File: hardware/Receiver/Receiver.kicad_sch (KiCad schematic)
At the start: 132 parts, among them J1 USB_C_Receptacle_USB2.0, J3 20021511-00006T4LF, J4 Conn_01x04, J6 JST_PH, Q1 2N7002, Q2 NMOS, Q3 NMOS, Q4 PMOS, SW1 Boot, SW1 Reset, SW3 1825027-8, U1 TPS22810DRV, U2 DMG6602SVTQ, U2 TPS22810DRV, U3 AZ1117-3.3, U3 DMG6602SVTQ, U4 TLV493DA1B6HTSA2, U6 BQ76905, U8 ESP32-S3-MINI-1-N8

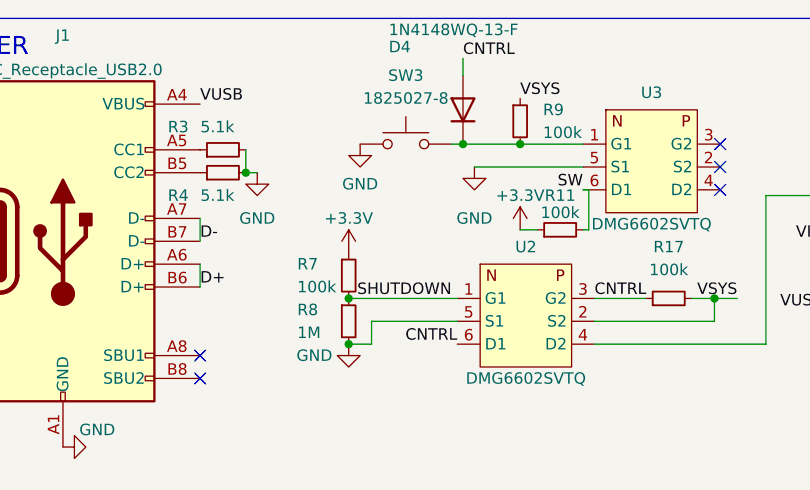
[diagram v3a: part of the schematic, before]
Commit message: add tvs diodes
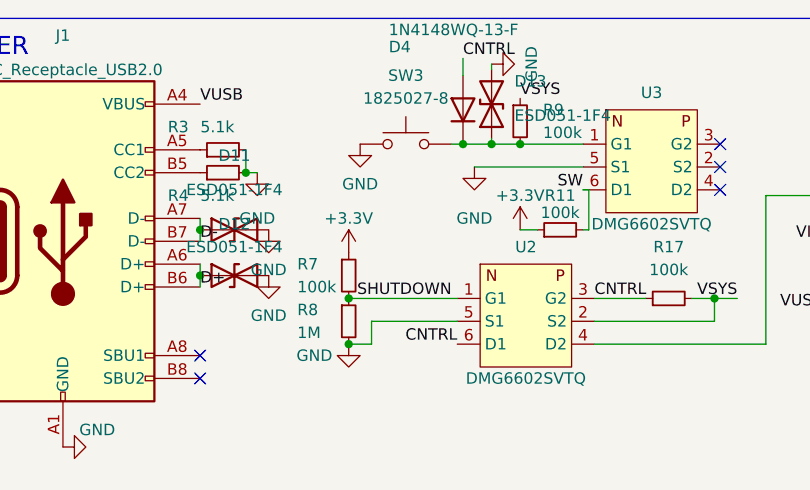
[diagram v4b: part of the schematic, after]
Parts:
- added D11, D12, D13: ESD051-1F4, Diode_SMD:D_0201_0603Metric, symbol Device:D_TVS
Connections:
- net D+: now also D12.1 (A1)
- net D-: now also D11.1 (A1)
- net GND: now also D11.2 (A2), D12.2 (A2), D13.2 (A2)
- net at D4.1 (K), R9.2, SW3.2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: now also D13.1 (A1)
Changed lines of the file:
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@@
   (junction (at 94.615 117.475) (diameter 0) (color 0 0 0 0)
   )
+  (junction (at 78.74 29.21) (diameter 0) (color 0 0 0 0)
+  )
   (junction (at 32.385 120.015) (diameter 0) (color 0 0 0 0)
   )
@@
   (junction (at 103.505 46.355) (diameter 0) (color 0 0 0 0)
   )
+  (junction (at 46.355 38.735) (diameter 0) (color 0 0 0 0)
+  )
   (junction (at 71.12 83.185) (diameter 0) (color 0 0 0 0)
   )
@@
   (junction (at 75.565 29.21) (diameter 0) (color 0 0 0 0)
   )
+  (junction (at 46.355 43.815) (diameter 0) (color 0 0 0 0)
+  )
   (junction (at 97.155 126.365) (diameter 0) (color 0 0 0 0)
   )
@@
     (stroke (width 0) (type default))
   )
-  (wire (pts (xy 75.565 29.21) (xy 81.915 29.21))
+  (wire (pts (xy 75.565 29.21) (xy 78.74 29.21))
     (stroke (width 0) (type default))
   )
@@
     (stroke (width 0) (type default))
   )
+  (wire (pts (xy 78.74 29.21) (xy 81.915 29.21))
+    (stroke (width 0) (type default))
+  )
   (wire (pts (xy 102.87 175.895) (xy 80.645 175.895))
     (stroke (width 0) (type default))
@@
     (stroke (width 0) (type default))
   )
+  (wire (pts (xy 46.355 38.735) (xy 46.355 40.005))
+    (stroke (width 0) (type default))
+  )
   (wire (pts (xy 39.37 141.605) (xy 43.18 141.605))
     (stroke (width 0) (type default))
@@
     (stroke (width 0) (type default))
   )
+  (wire (pts (xy 46.355 43.815) (xy 46.355 45.085))
+    (stroke (width 0) (type default))
+  )
   (wire (pts (xy 109.22 34.925) (xy 124.46 34.925))
     (stroke (width 0) (type default))
@@
     (stroke (width 0) (type default))
   )
-  (wire (pts (xy 46.355 37.465) (xy 46.355 40.005))
+  (wire (pts (xy 46.355 37.465) (xy 46.355 38.735))
     (stroke (width 0) (type default))
   )
@@
     (stroke (width 0) (type default))
   )
+  (wire (pts (xy 78.74 28.575) (xy 78.74 29.21))
+    (stroke (width 0) (type default))
+  )
   (wire (pts (xy 129.54 41.275) (xy 129.54 42.545))
     (stroke (width 0) (type default))
@@
     (stroke (width 0) (type default))
   )
-  (wire (pts (xy 46.355 42.545) (xy 46.355 45.085))
+  (wire (pts (xy 46.355 42.545) (xy 46.355 43.815))
     (stroke (width 0) (type default))
   )
@@
     (stroke (width 0) (type default))
   )
+  (wire (pts (xy 78.74 20.32) (xy 78.74 20.955))
+    (stroke (width 0) (type default))
+  )
   (wire (pts (xy 80.645 136.525) (xy 93.345 136.525))
     (stroke (width 0) (type default))
@@
     )
   )
+  (symbol (lib_id "power:GND") (at 53.975 38.735 0) (unit 1)
+    (in_bom yes) (on_board yes) (dnp no) (fields_autoplaced)
+    (property "Reference" "#PWR075" (at 53.975 45.085 0)
+      (effects (font (size 1.27 1.27)) hide)
+    )
+    (property "Value" "GND" (at 53.975 43.18 0)
+      (effects (font (size 1.27 1.27)))
+    )
+    (property "Footprint" "" (at 53.975 38.735 0)
+      (effects (font (size 1.27 1.27)) hide)
+    )
+    (property "Datasheet" "" (at 53.975 38.735 0)
+      (effects (font (size 1.27 1.27)) hide)
+    )
+    (pin "1")
+    (instances
+      (project "Receiver"
+        (path "/65c9fdc5-280c-4d5e-b4cf-324fcb70d6aa"
+          (reference "#PWR075") (unit 1)
+        )
+      )
+    )
+  )
   (symbol (lib_id "power:GND") (at 233.68 148.59 0) (unit 1)
     (in_bom yes) (on_board yes) (dnp no) (fields_autoplaced)
@@
     )
   )
+  (symbol (lib_id "Device:D_TVS") (at 50.165 38.735 0) (unit 1)
+    (in_bom yes) (on_board yes) (dnp no) (fields_autoplaced)
+    (property "Reference" "D11" (at 50.165 30.48 0)
+      (effects (font (size 1.27 1.27)))
+    )
+    (property "Value" "	\nESD051-1F4" (at 50.165 34.29 0)
+      (effects (font (size 1.27 1.27)))
+    )
+    (property "Footprint" "Diode_SMD:D_0201_0603Metric" (at 50.165 38.735 0)
+      (effects (font (size 1.27 1.27)) hide)
+    )
+    (property "Datasheet" "~" (at 50.165 38.735 0)
+      (effects (font (size 1.27 1.27)) hide)
+    )
+    (pin "1")
+    (pin "2")
+    (instances
+      (project "Receiver"
+        (path "/65c9fdc5-280c-4d5e-b4cf-324fcb70d6aa"
+          (reference "D11") (unit 1)
+        )
+      )
+    )
+  )
   (symbol (lib_id "power:+3.3V") (at 224.155 138.43 0) (unit 1)
     (in_bom yes) (on_board yes) (dnp no) (fields_autoplaced)
@@
     )
   )
+  (symbol (lib_id "power:GND") (at 78.74 20.32 90) (unit 1)
+    (in_bom yes) (on_board yes) (dnp no) (fields_autoplaced)
+    (property "Reference" "#PWR076" (at 85.09 20.32 0)
+      (effects (font (size 1.27 1.27)) hide)
+    )
+    (property "Value" "GND" (at 83.185 20.32 0)
+      (effects (font (size 1.27 1.27)))
+    )
+    (property "Footprint" "" (at 78.74 20.32 0)
+      (effects (font (size 1.27 1.27)) hide)
+    )
+    (property "Datasheet" "" (at 78.74 20.32 0)
+      (effects (font (size 1.27 1.27)) hide)
+    )
+    (pin "1")
+    (instances
+      (project "Receiver"
+        (path "/65c9fdc5-280c-4d5e-b4cf-324fcb70d6aa"
+          (reference "#PWR076") (unit 1)
+        )
+      )
+    )
+  )
   (symbol (lib_id "Switch:SW_Push") (at 23.495 89.535 90) (unit 1)
     (in_bom yes) (on_board yes) (dnp no)
@@
     )
   )
+  (symbol (lib_id "power:GND") (at 53.975 43.815 0) (unit 1)
+    (in_bom yes) (on_board yes) (dnp no) (fields_autoplaced)
+    (property "Reference" "#PWR074" (at 53.975 50.165 0)
+      (effects (font (size 1.27 1.27)) hide)
+    )
+    (property "Value" "GND" (at 53.975 48.26 0)
+      (effects (font (size 1.27 1.27)))
+    )
+    (property "Footprint" "" (at 53.975 43.815 0)
+      (effects (font (size 1.27 1.27)) hide)
+    )
+    (property "Datasheet" "" (at 53.975 43.815 0)
+      (effects (font (size 1.27 1.27)) hide)
+    )
+    (pin "1")
+    (instances
+      (project "Receiver"
+        (path "/65c9fdc5-280c-4d5e-b4cf-324fcb70d6aa"
+          (reference "#PWR074") (unit 1)
+        )
+      )
+    )
+  )
   (symbol (lib_id "power:GND") (at 140.97 165.735 0) (unit 1)
     (in_bom yes) (on_board yes) (dnp no) (fields_autoplaced)
@@
     )
   )
+  (symbol (lib_id "Device:D_TVS") (at 78.74 24.765 90) (unit 1)
+    (in_bom yes) (on_board yes) (dnp no) (fields_autoplaced)
+    (property "Reference" "D13" (at 81.28 22.225 90)
+      (effects (font (size 1.27 1.27)) (justify right))
+    )
+    (property "Value" "	\nESD051-1F4" (at 81.28 26.0349 90)
+      (effects (font (size 1.27 1.27)) (justify right))
+    )
+    (property "Footprint" "Diode_SMD:D_0201_0603Metric" (at 78.74 24.765 0)
+      (effects (font (size 1.27 1.27)) hide)
+    )
+    (property "Datasheet" "~" (at 78.74 24.765 0)
+      (effects (font (size 1.27 1.27)) hide)
+    )
+    (pin "1")
+    (pin "2")
+    (instances
+      (project "Receiver"
+        (path "/65c9fdc5-280c-4d5e-b4cf-324fcb70d6aa"
+          (reference "D13") (unit 1)
+        )
+      )
+    )
+  )
   (symbol (lib_id "Mechanical:MountingHole") (at 168.275 91.44 0) (unit 1)
     (in_bom yes) (on_board yes) (dnp no) (fields_autoplaced)
@@
         )
       )
+    )
+  )
+  (symbol (lib_id "Device:D_TVS") (at 50.165 43.815 0) (unit 1)
+    (in_bom yes) (on_board yes) (dnp no) (fields_autoplaced)
+    (property "Reference" "D12" (at 50.165 38.1 0)
+      (effects (font (size 1.27 1.27)))
+    )
+    (property "Value" "ESD051-1F4" (at 50.165 40.64 0)
+      (effects (font (size 1.27 1.27)))
+    )
+    (property "Footprint" "Diode_SMD:D_0201_0603Metric" (at 50.165 43.815 0)
+      (effects (font (size 1.27 1.27)) hide)
+    )
+    (property "Datasheet" "~" (at 50.165 43.815 0)
+      (effects (font (size 1.27 1.27)) hide)
+    )
+    (pin "1")
+    (pin "2")
+    (instances
+      (project "Receiver"
+        (path "/65c9fdc5-280c-4d5e-b4cf-324fcb70d6aa"
+          (reference "D12") (unit 1)
+        )
+      )

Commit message: PCB revision
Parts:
- removed C20, C23: 10u, Capacitor_SMD:C_0603_1608Metric, symbol Device:C_Small
- added D14, D15: TVN3V3B1S, Diode_SMD:D_0402_1005Metric, symbol Device:D_TVS
- added R21: 10k, Resistor_SMD:R_0402_1005Metric, symbol Device:R_Small
- C11, C13, C14, C15, C16, C17, C18, C19, C25, C26, C27, C3, C7: footprint Capacitor_SMD:C_0603_1608Metric -> Capacitor_SMD:C_0805_2012Metric
- D10, D4, D7, D8, D9: footprint Diode_SMD:D_SOD-123 -> Diode_SMD:D_SOD-323
- D11, D12, D13: value ESD051-1F4 -> TVN3V3B1S; footprint Diode_SMD:D_0201_0603Metric -> Diode_SMD:D_0402_1005Metric
- L1: footprint Inductor_SMD:L_Sunlord_MWSA0402S -> Inductor_SMD:L_1008_2520Metric
- R43, R44: footprint Resistor_SMD:R_0402_1005Metric -> Resistor_SMD:R_0603_1608Metric
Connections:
- net ESP_EN: now also D14.2 (A2)
- net ESP_IO0: now also D15.2 (A2)
- net GND: now also D14.1 (A1), D15.1 (A1), R21.1
- net at U8.22 (IO18/DAC2): now also R21.2
- no-connect marks 35 -> 34
